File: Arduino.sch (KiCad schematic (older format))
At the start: 0 parts

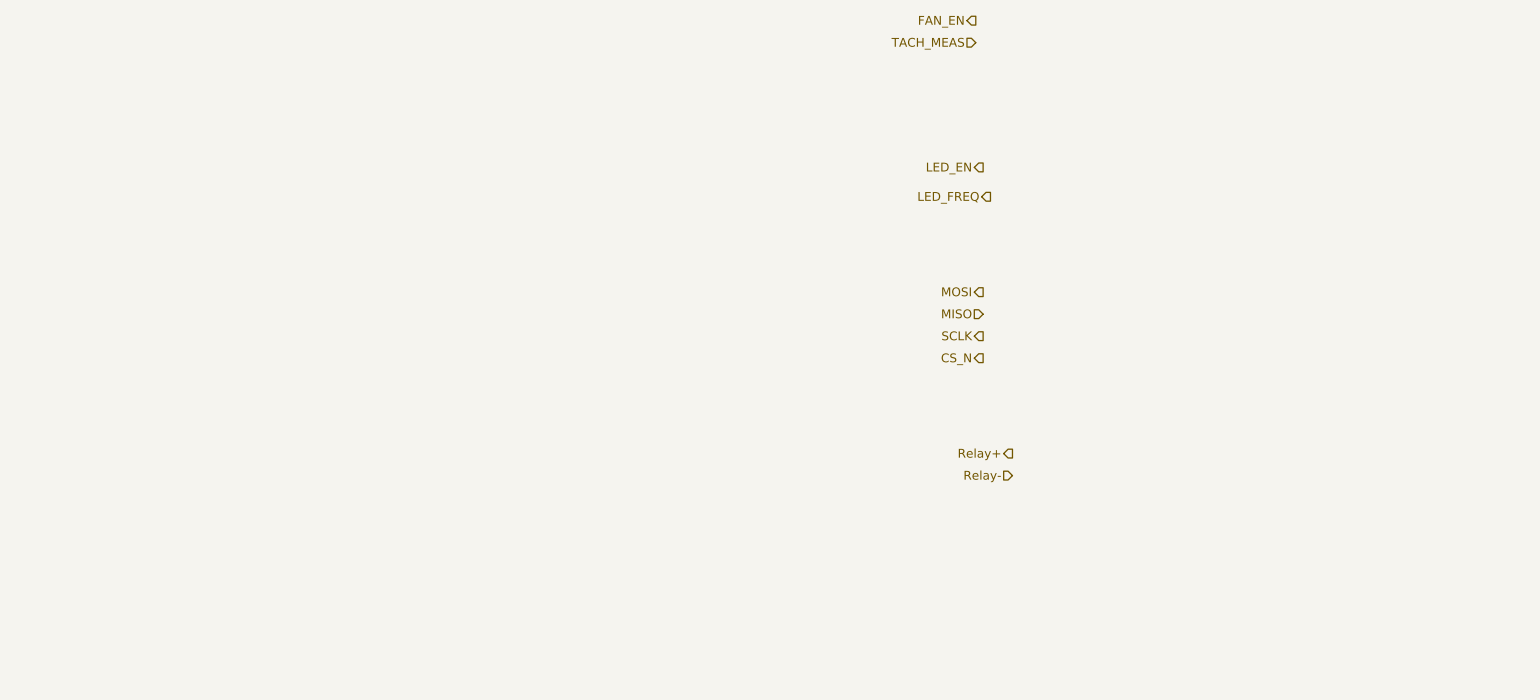
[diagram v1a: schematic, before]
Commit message: Added Arduino Module and Connected Top Level
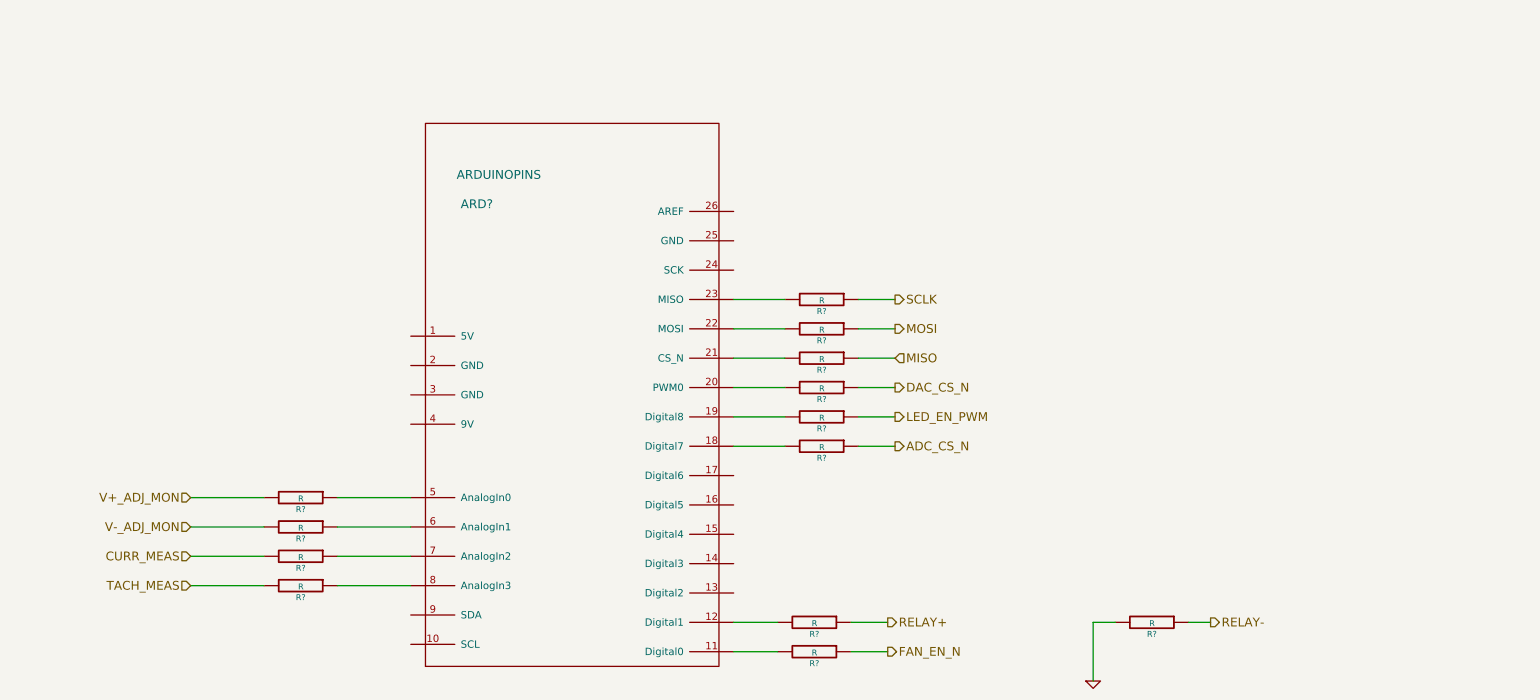
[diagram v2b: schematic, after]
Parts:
- added ARD?: ARDUINOPINS, symbol ARDUINOPINS
- added R? (x13): R, ~, symbol R
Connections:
- net MISO: now also R?.1
- net MOSI: now also R?.1
- net SCLK: now also R?.1
- net TACH_MEAS: now also R?.2
- new net: ARD?.11 (Digital0), R?.2
- new net: ARD?.12 (Digital1), R?.2
- new net: ARD?.18 (Digital7), R?.2
- new net: ARD?.19 (Digital8), R?.2
- new net: ARD?.20 (PWM0), R?.2
- new net: ARD?.21 (CS_N), R?.2
- new net: ARD?.22 (MOSI), R?.2
- new net: ARD?.23 (MISO), R?.2
- new net: ARD?.5 (AnalogIn0), R?.1
- new net: ARD?.6 (AnalogIn1), R?.1
- new net: ARD?.7 (AnalogIn2), R?.1
- new net: ARD?.8 (AnalogIn3), R?.1
- new net ADC_CS_N: R?.1
- new net CURR_MEAS: R?.2
- new net DAC_CS_N: R?.1
- new net FAN_EN_N: R?.1
- new net GND: R?.2
- new net LED_EN_PWM: R?.1
- new net RELAY+: R?.1
- new net RELAY-: R?.1
- new net V+_ADJ_MON: R?.2
- new net V-_ADJ_MON: R?.2

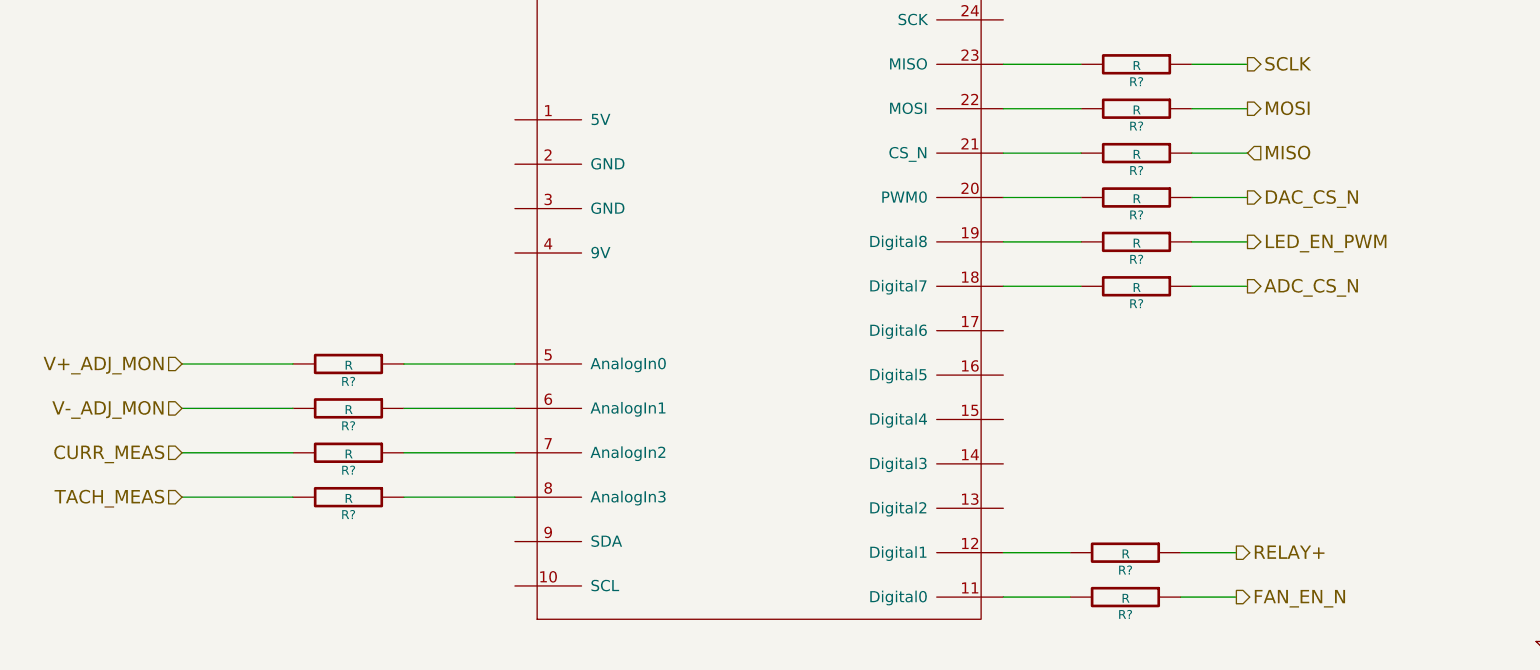
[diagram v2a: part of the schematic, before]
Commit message: Fan/Current Module Refactoring
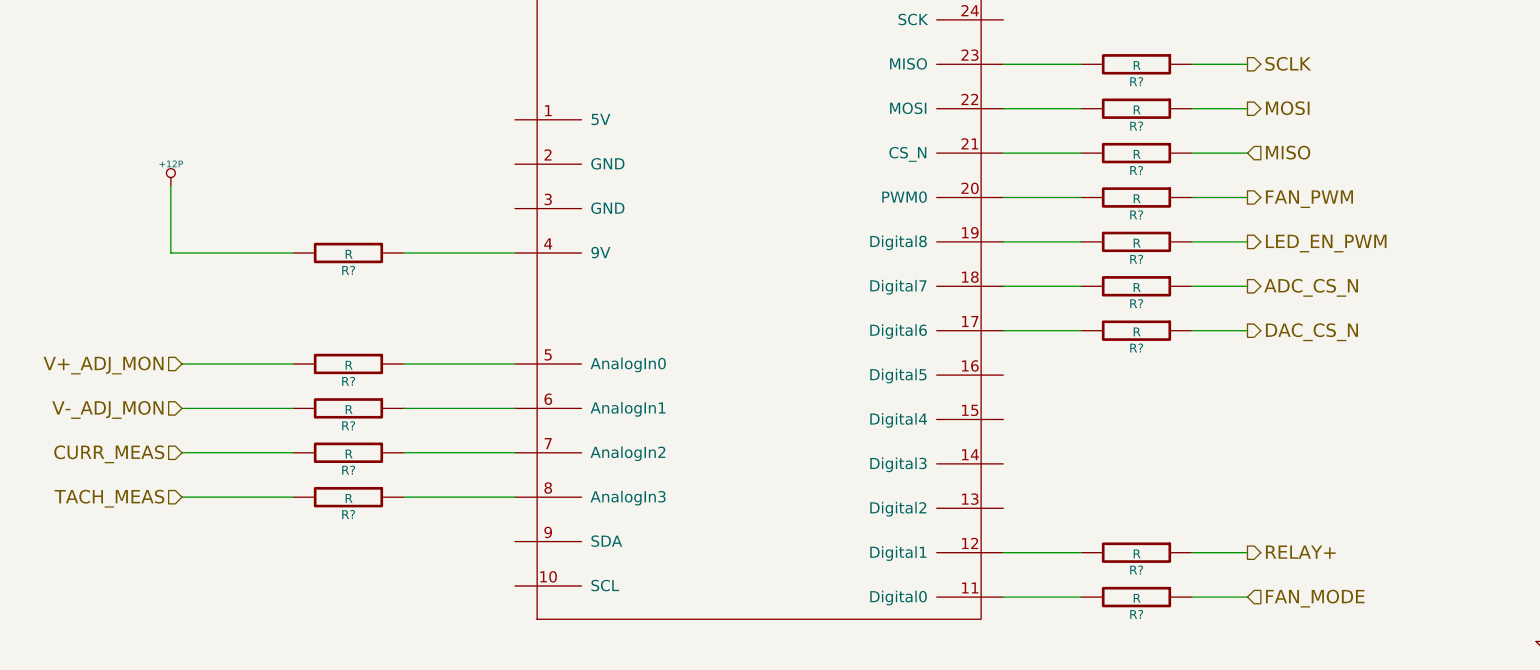
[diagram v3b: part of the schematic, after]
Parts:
- added R? (x2): R, ~, symbol R
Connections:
- net at ARD?.11 (Digital0): now also R?.2; no longer R?.2
- net at ARD?.17 (Digital6): now also R?.2
- net at ARD?.20 (PWM0): now also R?.2; no longer R?.2
- net at ARD?.4 (9V): now also R?.1
- net FAN_EN_N renamed FAN_PWM
- new net +12P: R?.2
- new net FAN_MODE: R?.1
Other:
- moved on the sheet: R?
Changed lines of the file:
@@
-EESchema Schematic File Version 2  date 9/22/2013 9:40:39 PM
+EESchema Schematic File Version 2  date 9/25/2013 9:41:11 PM
 LIBS:power
 LIBS:device
@@
 $Descr A4 11693 8268
 encoding utf-8
-Sheet 8 9
+Sheet 9 9
 Title ""
-Date "23 sep 2013"
+Date "26 sep 2013"
 Rev ""
 Comp ""
@@
 Comment4 ""
 $EndDescr
-Text HLabel 7100 5700 2    60   Output ~ 0
+Text HLabel 7150 5700 2    60   Output ~ 0
 RELAY+
 Text HLabel 9300 5700 2    60   Output ~ 0
@@
 Text HLabel 7150 3500 2    60   Output ~ 0
 SCLK
+Text HLabel 7150 4700 2    60   Output ~ 0
+DAC_CS_N
 Text HLabel 7150 4100 2    60   Output ~ 0
-DAC_CS_N
-Text HLabel 7100 5900 2    60   Output ~ 0
-FAN_EN_N
+FAN_PWM
 Text HLabel 2350 5450 0    60   Input ~ 0
 TACH_MEAS
@@
 L R R?
 U 1 1 52400F4A
-P 6600 5900
-F 0 "R?" V 6680 5900 40  0000 C CNN
-F 1 "R" V 6607 5901 40  0000 C CNN
-F 2 "~" V 6530 5900 30  0000 C CNN
-F 3 "~" H 6600 5900 30  0000 C CNN
-	1    6600 5900
-	0    1    1    0
-$EndComp
-Wire Wire Line
-	7100 5900 6850 5900
-Wire Wire Line
-	6350 5900 6050 5900
+P 6650 4100
+F 0 "R?" V 6730 4100 40  0000 C CNN
+F 1 "R" V 6657 4101 40  0000 C CNN
+F 2 "~" V 6580 4100 30  0000 C CNN
+F 3 "~" H 6650 4100 30  0000 C CNN
+	1    6650 4100
+	0    1    1    0
+$EndComp
+Wire Wire Line
+	7150 4100 6900 4100
+Wire Wire Line
+	6400 4100 6050 4100
 $Comp
 L R R?
 U 1 1 52400F79
-P 6600 5700
-F 0 "R?" V 6680 5700 40  0000 C CNN
-F 1 "R" V 6607 5701 40  0000 C CNN
-F 2 "~" V 6530 5700 30  0000 C CNN
-F 3 "~" H 6600 5700 30  0000 C CNN
-	1    6600 5700
-	0    1    1    0
-$EndComp
-Wire Wire Line
-	7100 5700 6850 5700
-Wire Wire Line
-	6350 5700 6050 5700
+P 6650 5700
+F 0 "R?" V 6730 5700 40  0000 C CNN
+F 1 "R" V 6657 5701 40  0000 C CNN
+F 2 "~" V 6580 5700 30  0000 C CNN
+F 3 "~" H 6650 5700 30  0000 C CNN
+	1    6650 5700
+	0    1    1    0
+$EndComp
+Wire Wire Line
+	7150 5700 6900 5700
+Wire Wire Line
+	6400 5700 6050 5700
 Wire Wire Line
 	8500 5700 8500 6100
@@
 L R R?
 U 1 1 52402D41
-P 6650 4100
-F 0 "R?" V 6730 4100 40  0000 C CNN
-F 1 "R" V 6657 4101 40  0000 C CNN
-F 2 "~" V 6580 4100 30  0000 C CNN
-F 3 "~" H 6650 4100 30  0000 C CNN
-	1    6650 4100
+P 6650 4700
+F 0 "R?" V 6730 4700 40  0000 C CNN
+F 1 "R" V 6657 4701 40  0000 C CNN
+F 2 "~" V 6580 4700 30  0000 C CNN
+F 3 "~" H 6650 4700 30  0000 C CNN
+	1    6650 4700
 	0    1    1    0
 $EndComp
@@
 	6900 3900 7150 3900
 Wire Wire Line
-	7150 4100 6900 4100
-Wire Wire Line
-	6400 4100 6050 4100
+	7150 4700 6900 4700
+Wire Wire Line
+	6400 4700 6050 4700
 $Comp
 L R R?
@@
 Wire Wire Line
 	7150 4500 6900 4500
+Text HLabel 7150 5900 2    60   Input ~ 0
+FAN_MODE
+$Comp
+L R R?
+U 1 1 5243CF0D
+P 6650 5900
+F 0 "R?" V 6730 5900 40  0000 C CNN
+F 1 "R" V 6657 5901 40  0000 C CNN
+F 2 "~" V 6580 5900 30  0000 C CNN
+F 3 "~" H 6650 5900 30  0000 C CNN
+	1    6650 5900
+	0    1    1    0
+$EndComp
+Wire Wire Line
+	7150 5900 6900 5900
+Wire Wire Line
+	6400 5900 6050 5900
+$Comp
+L R R?
+U 1 1 5243CF86
+P 3100 4350
+F 0 "R?" V 3180 4350 40  0000 C CNN
+F 1 "R" V 3107 4351 40  0000 C CNN
+F 2 "~" V 3030 4350 30  0000 C CNN
+F 3 "~" H 3100 4350 30  0000 C CNN
+	1    3100 4350
+	0    1    1    0
+$EndComp
+Wire Wire Line
+	3350 4350 3850 4350
+$Comp
+L +12P #PWR?
+U 1 1 5243CFCD
+P 2300 4050
+F 0 "#PWR?" H 2300 4020 30  0001 C CNN
+F 1 "+12P" H 2300 4150 30  0000 C CNN
+F 2 "~" H 2300 4050 60  0000 C CNN
+F 3 "~" H 2300 4050 60  0000 C CNN
+	1    2300 4050
+	1    0    0    -1
+$EndComp
+Wire Wire Line
+	2300 4050 2300 4350
+Wire Wire Line
+	2300 4350 2850 4350
 $EndSCHEMATC
